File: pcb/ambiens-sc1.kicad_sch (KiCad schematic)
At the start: 30 parts, among them J1 AQ FAN, J10 AQ_SENSOR_0x77, J11 PWR_BTN, J12 CTRL, J2 Heater Temp, J3 Heater Fan, J4 AQ Fan, J5 Heater, J7 PSU, J9 AQ_SENSOR_0x76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

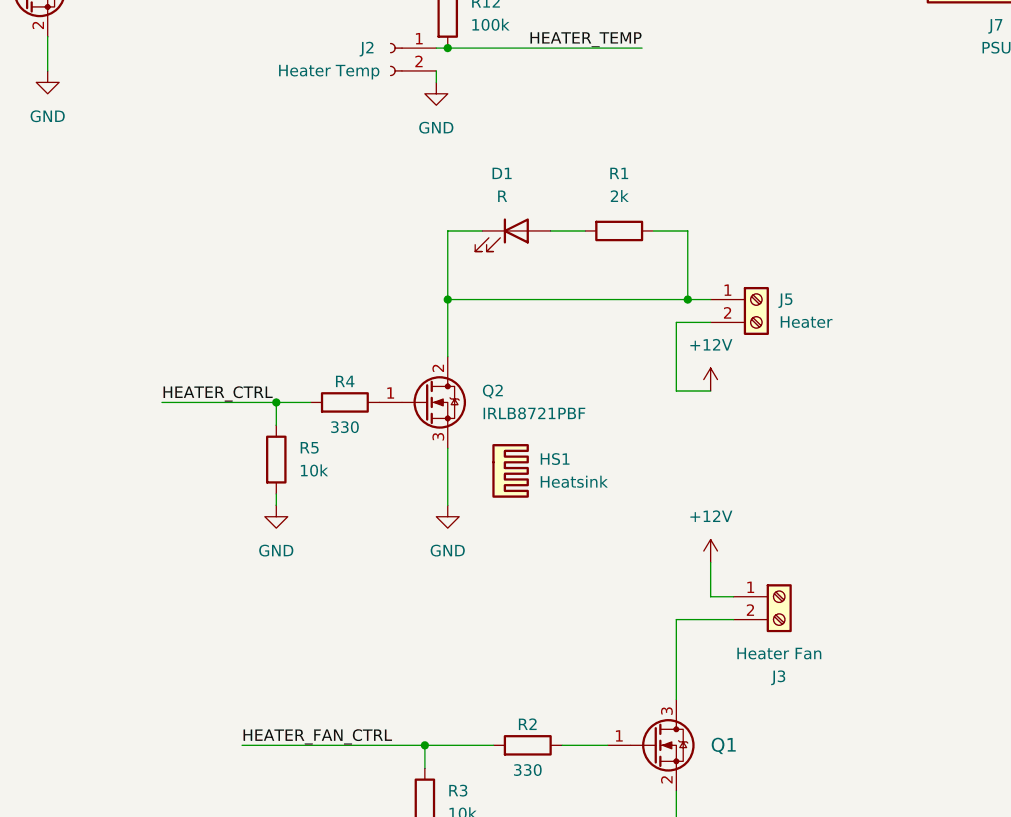
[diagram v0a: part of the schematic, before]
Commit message: Fix red led + label typo
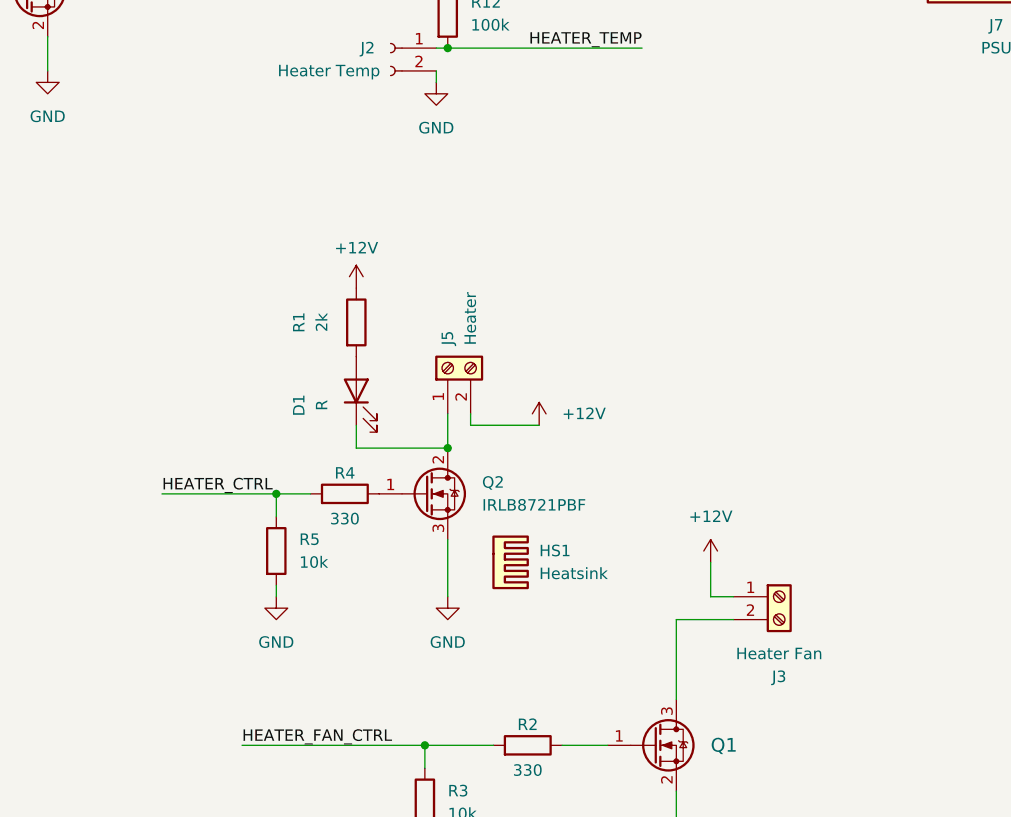
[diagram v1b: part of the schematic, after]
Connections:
- net +12V: now also R1.1
- net at D1.1 (K), J5.1 (Pin_1), Q2.2 (D): no longer R1.1
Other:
- moved on the sheet: D1, HS1, J5, Q2, R1, R4, R5
